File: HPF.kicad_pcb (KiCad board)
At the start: 4 copper layers, 100 x 100 mm, 153 parts, among them J1 CONN_COAXIAL, J3 CONN_COAXIAL, J4 CONN_01X13, Q1 BSS84, U2 PGA103+

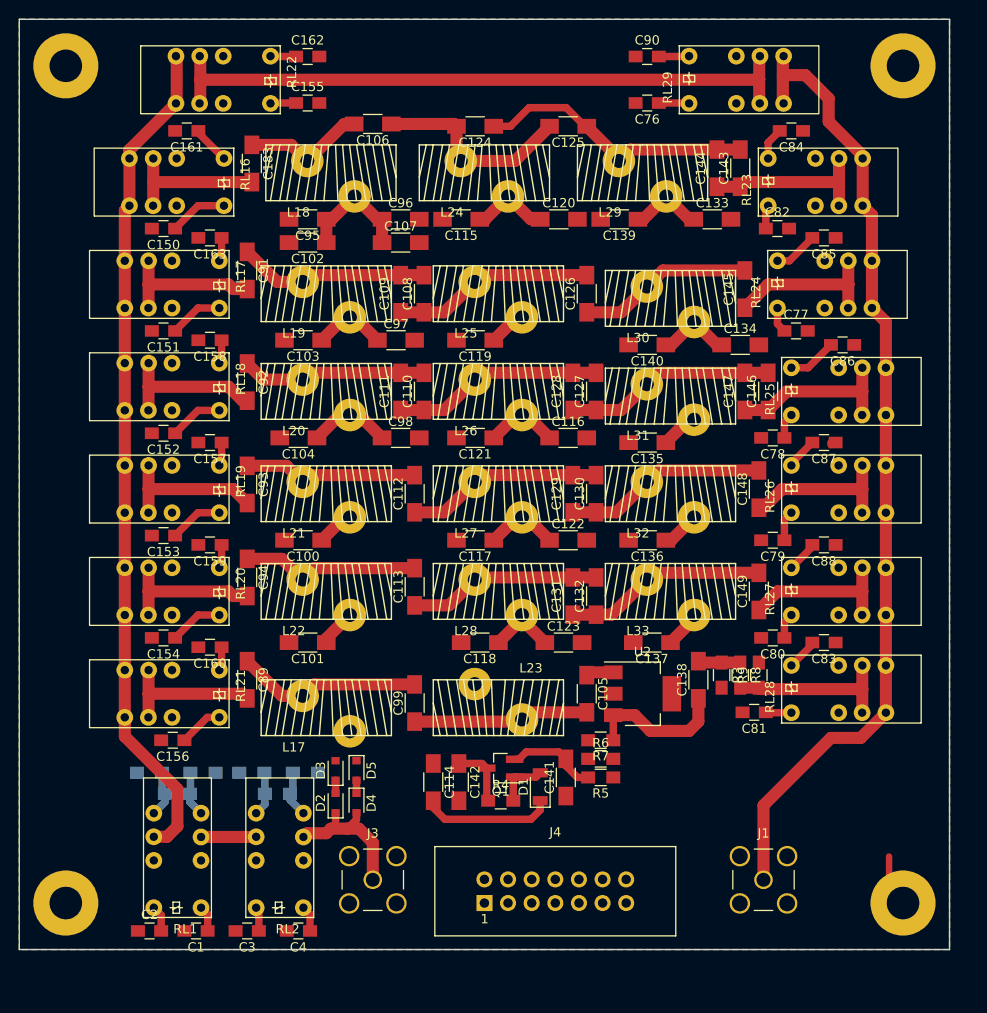
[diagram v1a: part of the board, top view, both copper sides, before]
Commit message: silkmask cleanup and comments added
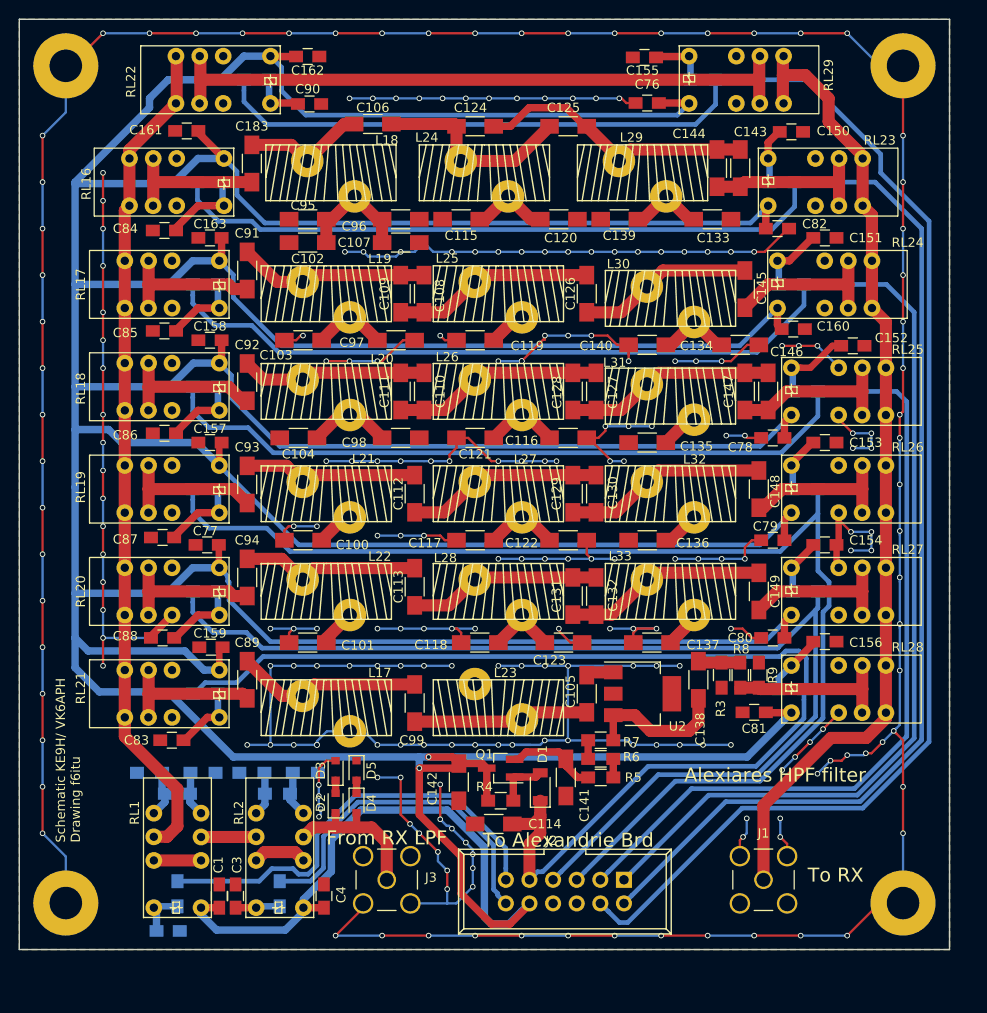
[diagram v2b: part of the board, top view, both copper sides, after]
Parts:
- removed J4: CONN_01X13, Connectors:IDC_Header_Straight_14pins
- added J2: Conn_01x12, Connect:IDC_Header_Straight_12pins, F.Cu at (155.0, 105.0)
- added L1: Choke, Inductors_SMD:L_0805_HandSoldering, B.Cu at (107.0, 106.5)
- added L10: Choke, Inductors_SMD:L_0805_HandSoldering, B.Cu at (172.0, 30.0)
- added L11: Choke, Inductors_SMD:L_0805_HandSoldering, B.Cu at (173.0, 41.0)
- added L12: Choke, Inductors_SMD:L_0805_HandSoldering, B.Cu at (174.5, 63.0)
- added L13: Choke, Inductors_SMD:L_0805_HandSoldering, B.Cu at (174.5, 74.0)
- added L14: Choke, Inductors_SMD:L_0805_HandSoldering, B.Cu at (173.0, 84.5)
- added L15: Choke, Inductors_SMD:L_0805_HandSoldering, B.Cu at (174.5, 52.5)
- added L16: Choke, Inductors_SMD:L_0805_HandSoldering, B.Cu at (118.0, 106.5)
- added L2: Choke, Inductors_SMD:L_0805_HandSoldering, B.Cu at (110.5, 30.0)
- added L3: Choke, Inductors_SMD:L_0805_HandSoldering, B.Cu at (110.0, 41.0)
- added L4: Choke, Inductors_SMD:L_0805_HandSoldering, B.Cu at (110.0, 63.0)
- added L5: Choke, Inductors_SMD:L_0805_HandSoldering, B.Cu at (110.0, 74.0)
- added L6: Choke, Inductors_SMD:L_0805_HandSoldering, B.Cu at (110.0, 85.0)
- added L7: Choke, Inductors_SMD:L_0805_HandSoldering, B.Cu at (110.0, 52.0)
- added L8: Choke, Inductors_SMD:L_0805_HandSoldering, B.Cu at (115.5, 19.0)
- added L9: Choke, Inductors_SMD:L_0805_HandSoldering, B.Cu at (163.5, 19.0)
- C2: moved to B.Cu
- moved C152 74.7 mm to (179.6, 47.6), turned to 0 degrees
- moved C86 73.5 mm to (105.6, 57.0), turned to 0 degrees
- moved C87 71.8 mm to (105.4, 68.2), turned to 0 degrees
- moved C151 71.8 mm to (176.6, 36.0), turned to 0 degrees
- moved C153 71.8 mm to (176.6, 58.0), turned to 0 degrees
- moved C154 71.8 mm to (176.6, 69.0), turned to 0 degrees
- moved C88 71.8 mm to (105.4, 79.0), turned to 0 degrees
- moved C85 71.6 mm to (105.6, 46.0), turned to 0 degrees
- moved C160 71.4 mm to (173.2, 45.8), turned to 0 degrees
- moved C156 70.9 mm to (176.6, 79.4), turned to 0 degrees
- moved C83 70.9 mm to (106.4, 90.0), turned to 0 degrees
- moved C150 68.3 mm to (173.0, 24.6), turned to 0 degrees
- moved C84 68.2 mm to (105.6, 35.2), turned to 0 degrees
- moved C77 67.3 mm to (110.2, 69.0), turned to 180 degrees
- moved C90 36.7 mm to (121.2, 21.6), turned to 180 degrees
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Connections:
- net Att1 renamed Net-(C3-Pad1)
- net Att2 renamed Net-(C2-Pad2)
- C142 pad 1: +5V -> +12V
- C150 pad 1: 1.5HPF -> Net-(C150-Pad1)
- C151 pad 1: 6.5HPF -> Net-(C151-Pad1)
- C152 pad 1: 9.5HPF -> Net-(C152-Pad1)
- C153 pad 1: 13HPF -> Net-(C153-Pad1)
- C154 pad 1: 20HPF -> Net-(C154-Pad1)
- C155 pad 1: HPF_ByPass -> Net-(C155-Pad1)
- C156 pad 1: 6mLNA -> Net-(C156-Pad1)
- C83 pad 2: 6mLNA -> Net-(C83-Pad2)
- C84 pad 2: 1.5HPF -> Net-(C84-Pad2)
- C85 pad 2: 6.5HPF -> Net-(C85-Pad2)
- C86 pad 2: 9.5HPF -> Net-(C86-Pad2)
- C87 pad 2: 13HPF -> Net-(C87-Pad2)
- C88 pad 2: 20HPF -> Net-(C88-Pad2)
- C90 pad 2: HPF_ByPass -> Net-(C90-Pad2)
- Q1 pad 3: +5V -> +12V
- R4 pad 1: +5V -> +12V
- RL16 pad 12: 1.5HPF -> Net-(C84-Pad2)
- RL17 pad 12: 6.5HPF -> Net-(C85-Pad2)
- RL18 pad 12: 9.5HPF -> Net-(C86-Pad2)
- RL19 pad 12: 13HPF -> Net-(C87-Pad2)
- RL20 pad 12: 20HPF -> Net-(C88-Pad2)
- RL21 pad 12: 6mLNA -> Net-(C83-Pad2)
- RL22 pad 12: HPF_ByPass -> Net-(C90-Pad2)
- RL23 pad 12: 1.5HPF -> Net-(C150-Pad1)
- RL24 pad 12: 6.5HPF -> Net-(C151-Pad1)
- RL25 pad 12: 9.5HPF -> Net-(C152-Pad1)
- RL26 pad 12: 13HPF -> Net-(C153-Pad1)
- RL27 pad 12: 20HPF -> Net-(C154-Pad1)
- RL28 pad 12: 6mLNA -> Net-(C156-Pad1)
- RL29 pad 12: HPF_ByPass -> Net-(C155-Pad1)
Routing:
- net GND: track 2.92 -> 865.8 mm, vias 0 -> 243
- net +12V: track 45.5 -> 785.3 mm, vias 0 -> 2
- net HPF_ByPass: track 6.03 -> 188.2 mm
- net 1.5HPF: track 9.75 -> 181.1 mm
- net 6.5HPF: track 10.5 -> 170.7 mm
- net 9.5HPF: track 11.0 -> 161.3 mm
- net 13HPF: track 9.16 -> 132.2 mm
- net 20HPF: track 9.16 -> 121.9 mm
- net 6mLNA: track 22.3 -> 124.0 mm
- net Att2: track 0.00 -> 47.3 mm
- net Att1: track 0.00 -> 37.2 mm
- net Net-(C152-Pad1): track 0.00 -> 9.93 mm
- net Net-(C84-Pad2): track 0.00 -> 8.87 mm
- net Net-(C88-Pad2): track 0.00 -> 8.37 mm
- net Net-(C87-Pad2): track 0.00 -> 8.37 mm
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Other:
- board text added: "+"
- board text added: "6.5 hpf 1.5 hpf ByPass"
- board text added: "6m/LNA 20hpf 13hpf 9.5hpf"
- board text added: "Alexiares HPF filter"
- board text added: "Att2 Att1"
- board text added: "From RX LPF"
- board text added: "Gnd"
- board text added: "Schematic KE9H/ VK6APH Drawing f6itu"
- board text added: "To Alexandrie Brd"
- board text added: "To RX"
- board text added: "to lpf 60MHz/ PS-RX switch"

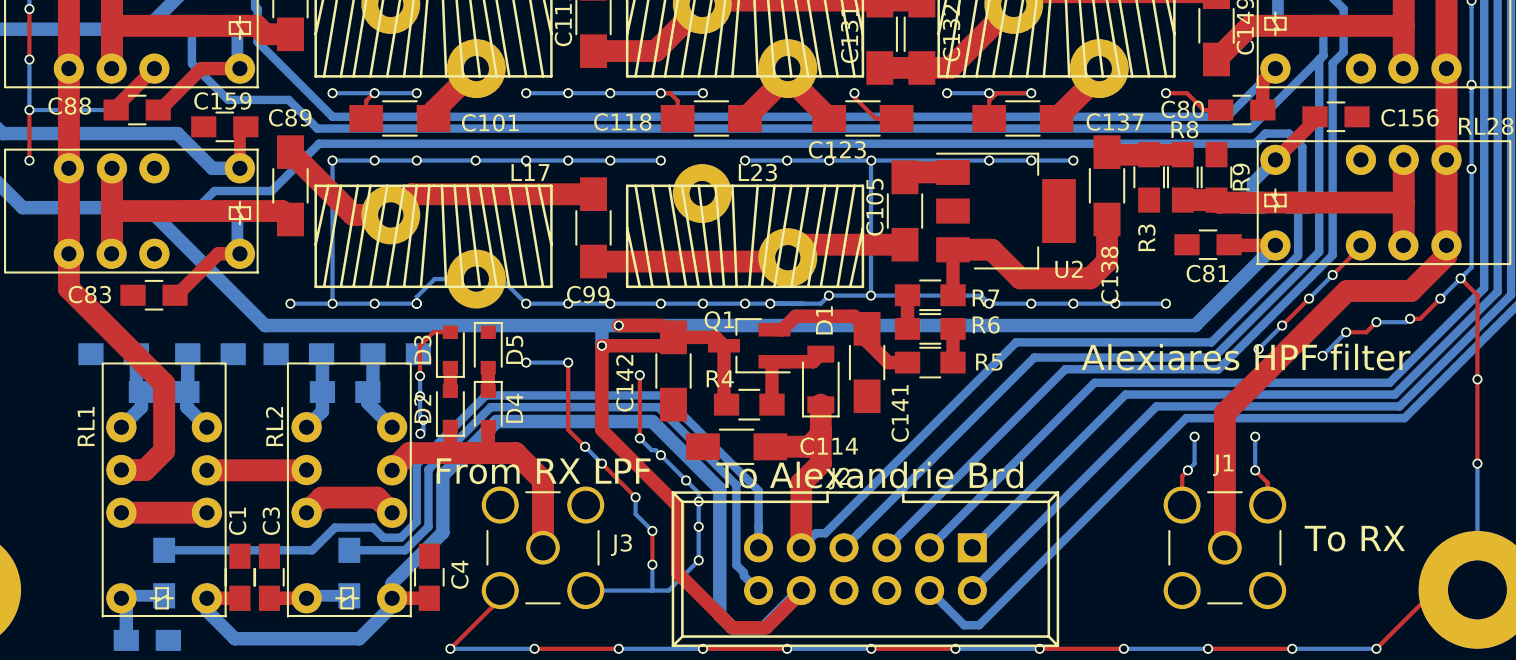
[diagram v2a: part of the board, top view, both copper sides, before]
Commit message: New LNA, silkmask modified
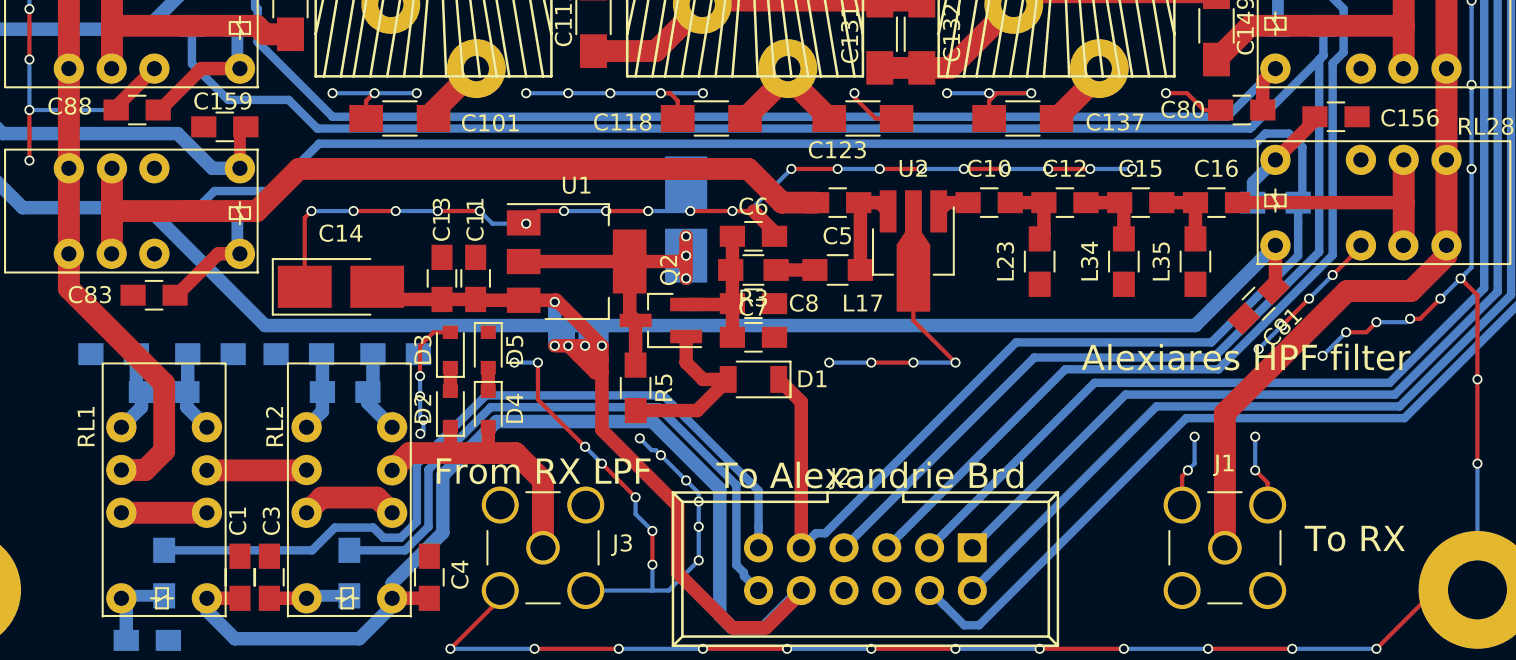
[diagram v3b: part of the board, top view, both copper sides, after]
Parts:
- removed C105, C89, C99: .1n, Capacitors_SMD:C_1206_HandSoldering
- removed C114, C138, C141, C142: 100n, Capacitors_SMD:C_1206_HandSoldering
- removed Q1: BSS84, TO_SOT_Packages_SMD:SOT-23_Handsoldering
- removed R4: 10k, Resistors_SMD:R_0805_HandSoldering
- removed R6, R7: 62, Resistors_SMD:R_0805_HandSoldering
- removed R8: 30R, Resistors_SMD:R_0805_HandSoldering
- removed R9: 100R, Resistors_SMD:R_0805_HandSoldering
- added C10: 100p, Capacitors_SMD:C_0805_HandSoldering, F.Cu at (156.0, 84.5)
- added C11: 10p, Capacitors_SMD:C_0805_HandSoldering, F.Cu at (125.5, 89.0)
- added C12: 60p, Capacitors_SMD:C_0805_HandSoldering, F.Cu at (160.5, 84.5)
- added C13: 100p, Capacitors_SMD:C_0805_HandSoldering, F.Cu at (123.5, 89.0)
- added C14: 10uf, Capacitors_Tantalum_SMD:CP_Tantalum_Case-B_EIA-3528-21_Hand, F.Cu at (117.5, 89.5)
- added C15: 60p, Capacitors_SMD:C_0805_HandSoldering, F.Cu at (165.0, 84.5)
- added C16: 100p, Capacitors_SMD:C_0805_HandSoldering, F.Cu at (169.5, 84.5)
- added C5: 10n, Capacitors_SMD:C_0805_HandSoldering, F.Cu at (147.0, 84.5)
- added C6: 10n, Capacitors_SMD:C_0805_HandSoldering, F.Cu at (142.0, 86.5)
- added C7: 100n, Capacitors_SMD:C_0805_HandSoldering, F.Cu at (142.0, 92.5)
- added C8: 1n, Capacitors_SMD:C_0805_HandSoldering, F.Cu at (142.0, 90.5)
- added C9: 10uf, Capacitors_Tantalum_SMD:CP_Tantalum_Case-B_EIA-3528-21_Hand, B.Cu at (138.0, 85.5)
- added L34: 220n, Inductors_SMD:L_0805_HandSoldering, F.Cu at (164.0, 88.0)
- added L35: 220n, Inductors_SMD:L_0805_HandSoldering, F.Cu at (168.2, 88.0)
- added Q2: zvp2106G, TO_SOT_Packages_SMD:SOT-23_Handsoldering, F.Cu at (136.5, 91.5)
- added U1: AP1117-50, TO_SOT_Packages_SMD:SOT-223-3_TabPin2, F.Cu at (131.5, 88.0)
- D1: value ZPV21 -> diode
- L17: value 330nH -> 220n; footprint T50:T50_V_THT -> Inductors_SMD:L_0805_HandSoldering
- L23: value 330n -> 220n; footprint T50:T50_V_THT -> Inductors_SMD:L_0805_HandSoldering
- R3: value 100R -> 18
- R5: value 62 -> 10k
- U2: footprint TO_SOT_Packages_SMD:SOT-223 -> TO_SOT_Packages_SMD:SOT-89-3_Handsoldering
- moved R3 24.1 mm to (142.0, 88.5), turned to 180 degrees
- moved L17 24.1 mm to (147.0, 88.5), turned to 180 degrees
- moved L23 17.6 mm to (159.0, 88.0), turned to 270 degrees
- moved R5 17.6 mm to (135.0, 95.5), turned to 270 degrees
- moved U2 5.85 mm to (151.5, 87.0), turned to 270 degrees
- moved C81 4.61 mm to (172.0, 90.5), turned to 225 degrees
- moved D1 4.00 mm to (142.0, 95.0), turned to 180 degrees
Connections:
- L17 pad 1: Net-(C89-Pad1) -> Net-(C5-Pad1)
- L17 pad 2: GND -> Net-(L17-Pad2)
- R3 pad 1: Net-(C138-Pad2) -> Net-(L17-Pad2)
- R3 pad 2: GND -> Net-(C6-Pad1)
- R5 pad 2: Net-(C141-Pad2) -> Net-(D1-Pad2)
- U2 pad 3: Net-(C138-Pad1) -> Net-(C5-Pad1)
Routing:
- net GND: track 865.8 -> 822.2 mm, vias 243 -> 232
- net Net-(C5-Pad2): track 15.9 -> 48.8 mm
- net Net-(C89-Pad1): track 20.1 -> 0.00 mm
- net Net-(C9-Pad2): track 2.00 -> 21.1 mm, vias 0 -> 3
- net Net-(C138-Pad1): track 15.5 -> 0.00 mm
- net Net-(C10-Pad1): track 19.3 -> 4.25 mm
- net +12V: track 785.3 -> 797.4 mm, vias 2 -> 5
- net Net-(C141-Pad2): track 9.81 -> 0.00 mm
- net Net-(C6-Pad1): track 0.00 -> 8.77 mm
- net Net-(C5-Pad1): track 0.00 -> 6.01 mm
- net Net-(D1-Pad2): track 5.55 -> 10.7 mm
- net Net-(C138-Pad2): track 4.56 -> 0.00 mm
- net Net-(C12-Pad1): track 0.00 -> 4.25 mm
- net Net-(C15-Pad1): track 0.00 -> 4.15 mm
- net Net-(C16-Pad1): track 18.3 -> 15.0 mm
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
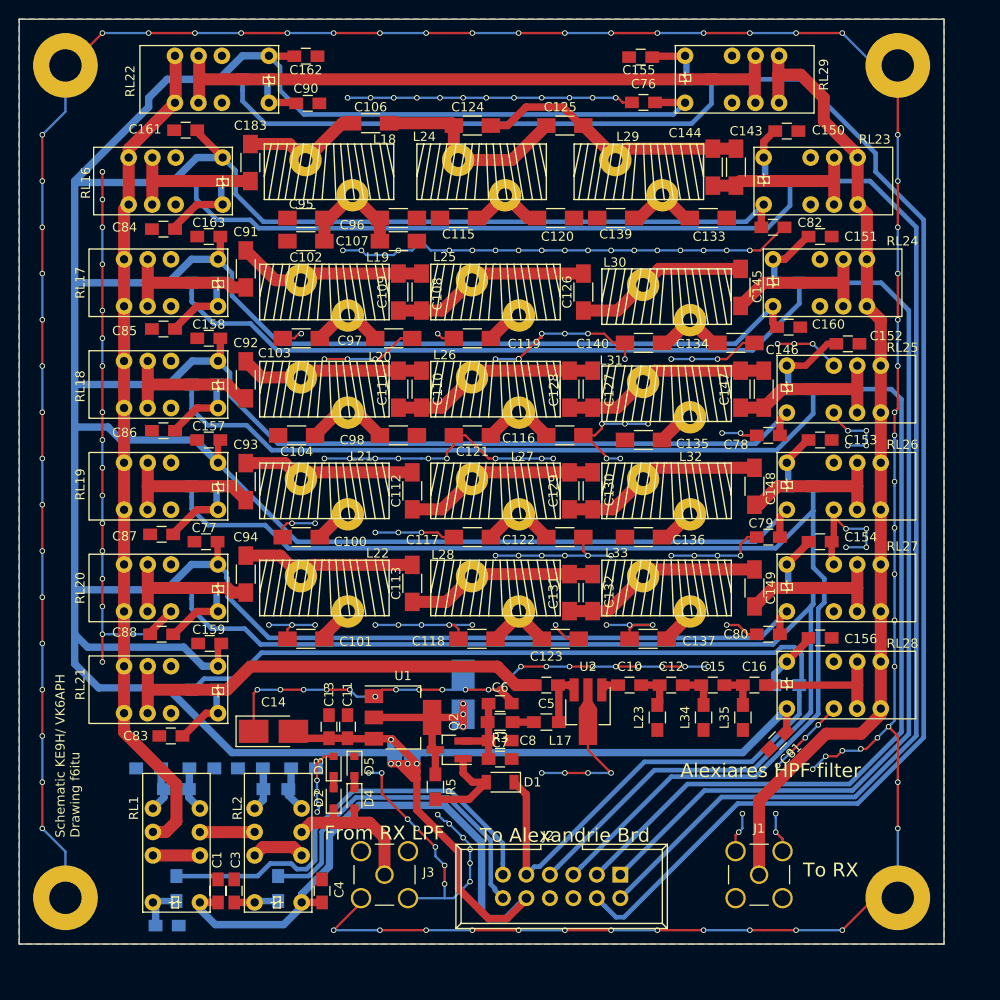
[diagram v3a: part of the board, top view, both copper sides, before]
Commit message: edge SMA added, main connector shifted
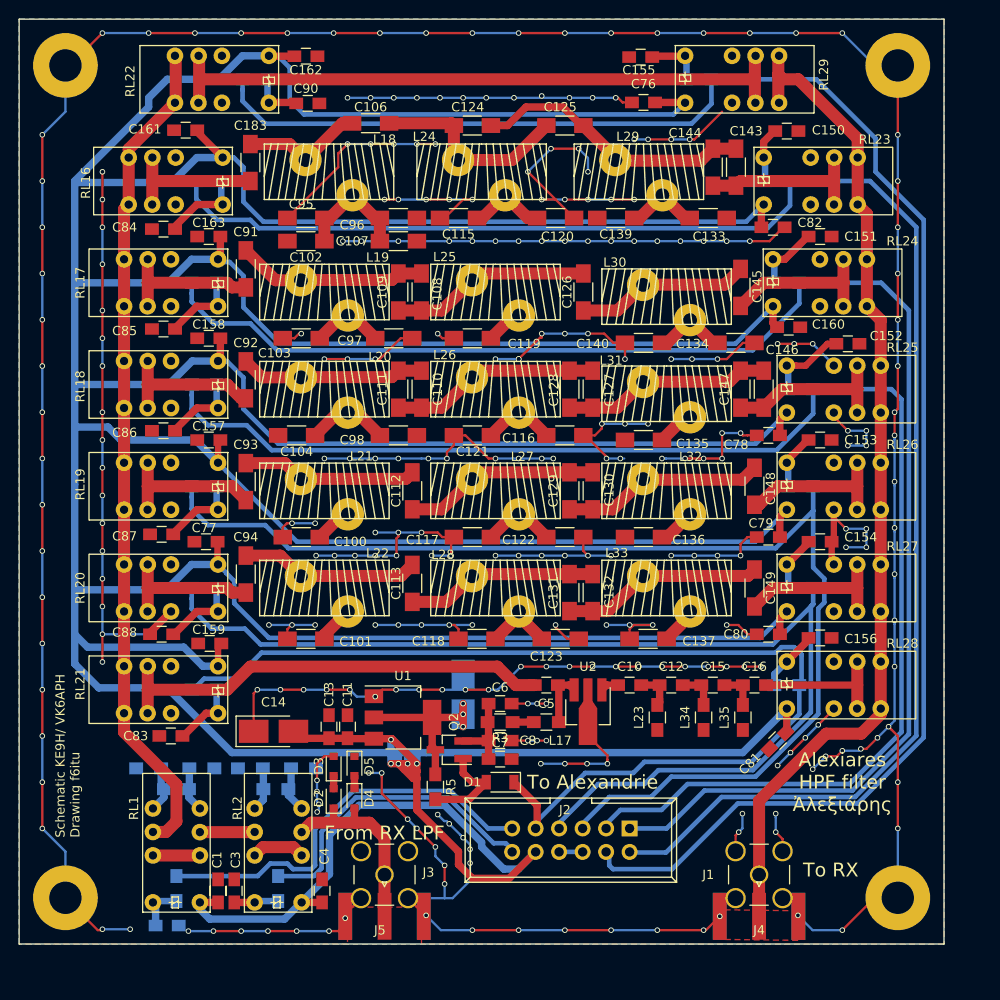
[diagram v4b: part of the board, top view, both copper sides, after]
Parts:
- added J4: CONN_COAXIAL, Connector_Coaxial:SMA_Amphenol_132289_EdgeMount, F.Cu at (170.0, 109.5)
- added J5: CONN_COAXIAL, Connector_Coaxial:SMA_Amphenol_132289_EdgeMount, F.Cu at (129.5, 109.5)
- moved J2 5.10 mm to (156.0, 100.0)
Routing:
- net GND: track 822.2 -> 930.0 mm, vias 232 -> 277
- net (no net): track 1.77 -> 12.5 mm, vias 3 -> 7
- net 6mLNA: track 122.0 -> 114.8 mm
- net +12V: track 797.4 -> 791.5 mm
- net Net-(D2-Pad1): track 17.3 -> 22.0 mm
- net Att1: track 37.2 -> 33.1 mm
- net Net-(J1-Pad1): track 105.3 -> 109.3 mm
- net 1.5HPF: track 181.1 -> 178.0 mm
- net Att2: track 47.3 -> 44.3 mm
- net 6.5HPF: track 170.7 -> 167.8 mm
- net 9.5HPF: track 161.3 -> 158.5 mm
- net 13HPF: track 132.2 -> 129.4 mm
- net 20HPF: track 121.9 -> 119.1 mm
- net HPF_ByPass: track 188.2 -> 186.6 mm
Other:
- board text added: "Alexiares HPF filter Ἀλεξιάρης"
- board text added: "To Alexandrie"
- board text removed: "Alexiares HPF filter"
- board text removed: "Pure Signal"
- board text removed: "RX1_Line"
- board text removed: "To Alexandrie Brd"

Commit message: changed sma footprint, gerber done
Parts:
- J4, J5: footprint Connector_Coaxial:SMA_Amphenol_132289_EdgeMount -> SMA_PINS:SMA_EDGE_NRW
- moved J4 1.00 mm to (170.0, 110.5)
- moved J5 1.00 mm to (129.5, 110.5)
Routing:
- net GND: track 930.0 -> 963.9 mm
